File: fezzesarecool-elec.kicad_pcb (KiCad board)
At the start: 2 copper layers, 65 x 56 mm, 62 parts, among them J1 Conn_sel, J14 Conn_LEDs, J15 Audio_input, J18 alim_jacky, J2 Conn_start, J3 CAN_conn, J4 CAN_conn, J5 Conn_01x02, J6 Conn_01x10, J7 alim_5V, P1 Conn_02x20_Odd_Even, Q1 NMOS-T252, Q2 NMOS-T252, Q3 NMOS-T252, U1 MCP2515-EST, U11 MC34152, U12 MC34152, U13 LM4991, U2 TCAN332, U3 SN74AHC1G08, Y1 Crystal_8MHz

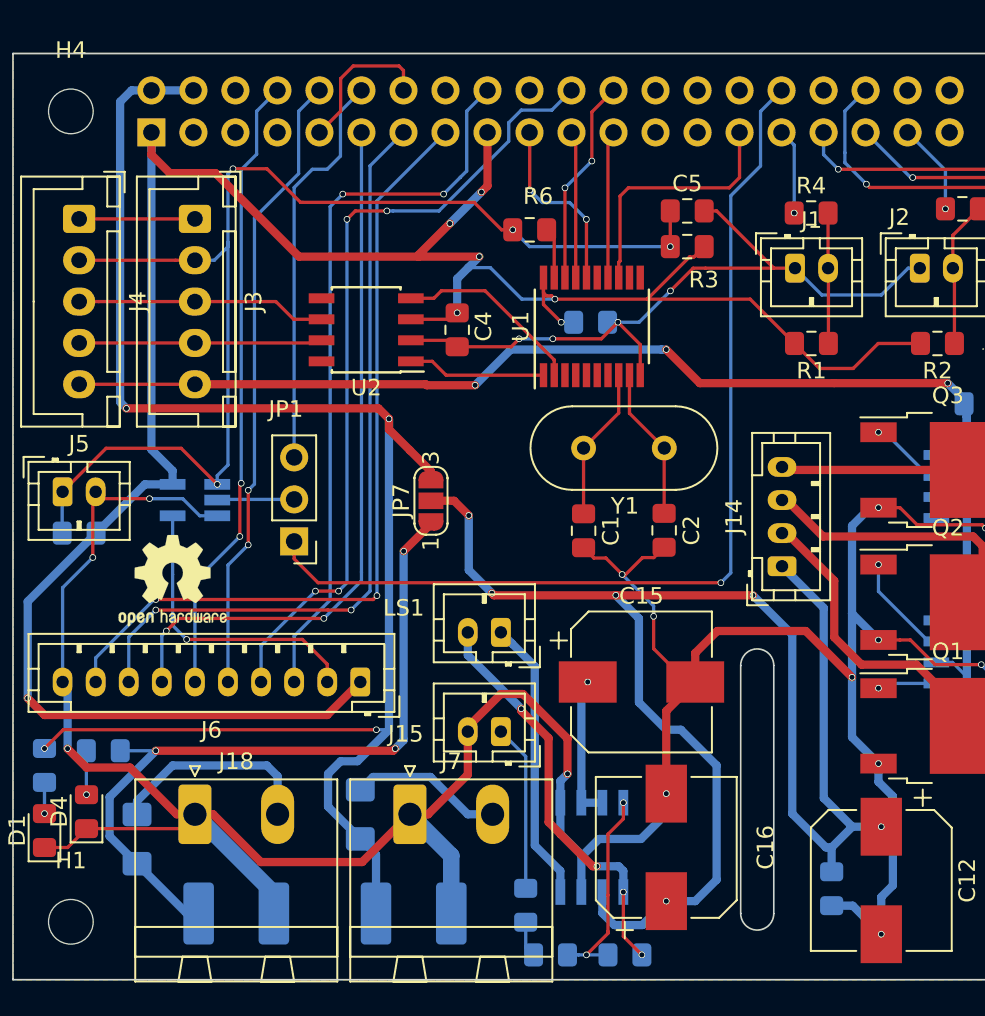
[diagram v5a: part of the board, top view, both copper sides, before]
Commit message: power  tracks corrected
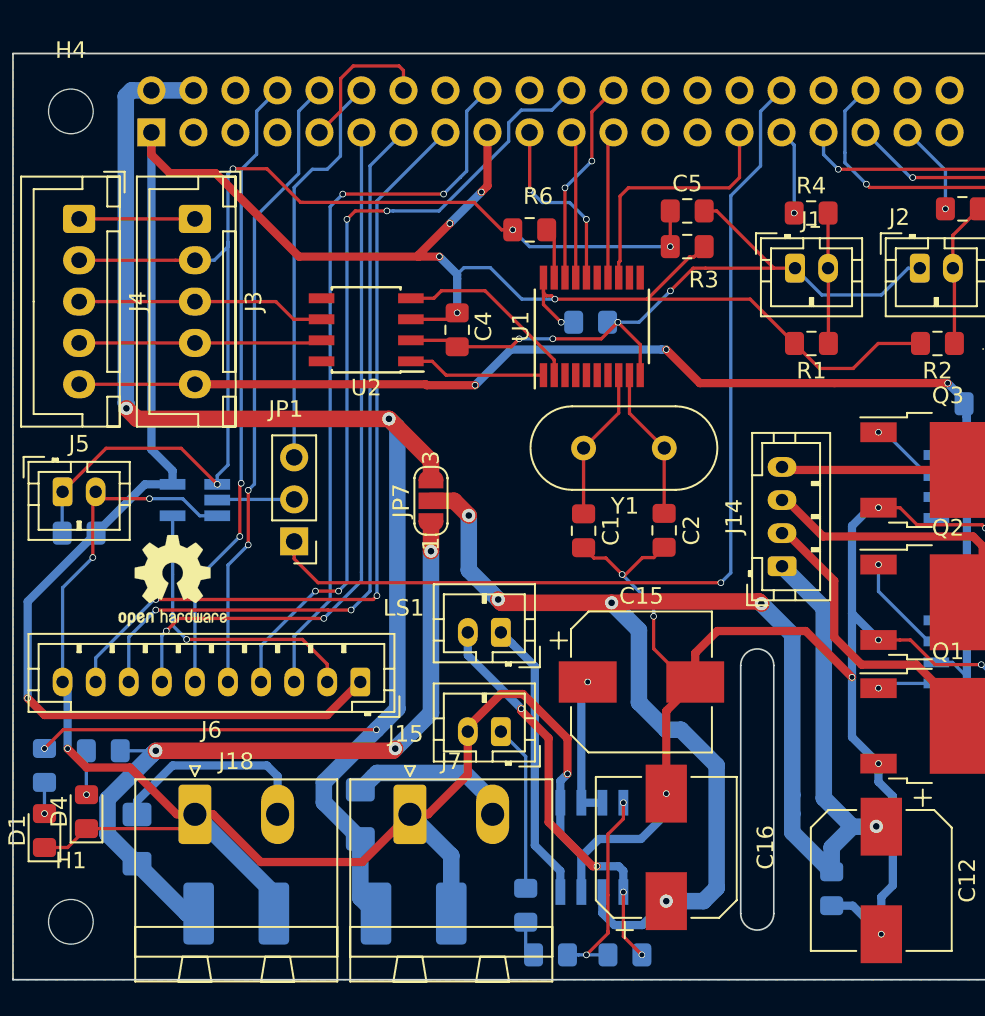
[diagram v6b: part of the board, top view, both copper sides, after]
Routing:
- net +5VD: track 93.6 -> 96.3 mm
- net +3V3: track 141.5 -> 139.8 mm
- net +5V: track 98.8 -> 97.7 mm
- net Net-(F1-Pad1): track 9.26 -> 9.92 mm

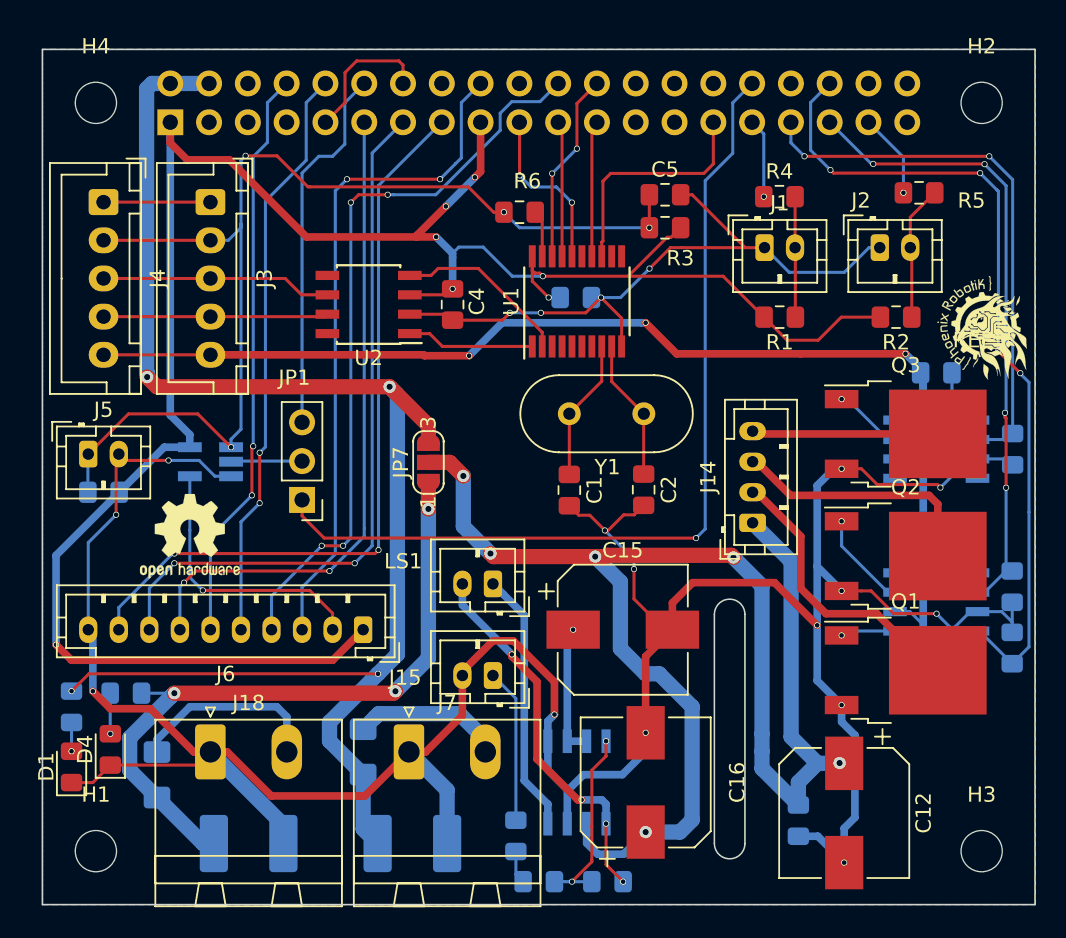
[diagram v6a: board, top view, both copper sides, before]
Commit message: coins arrondis, fix connecteur
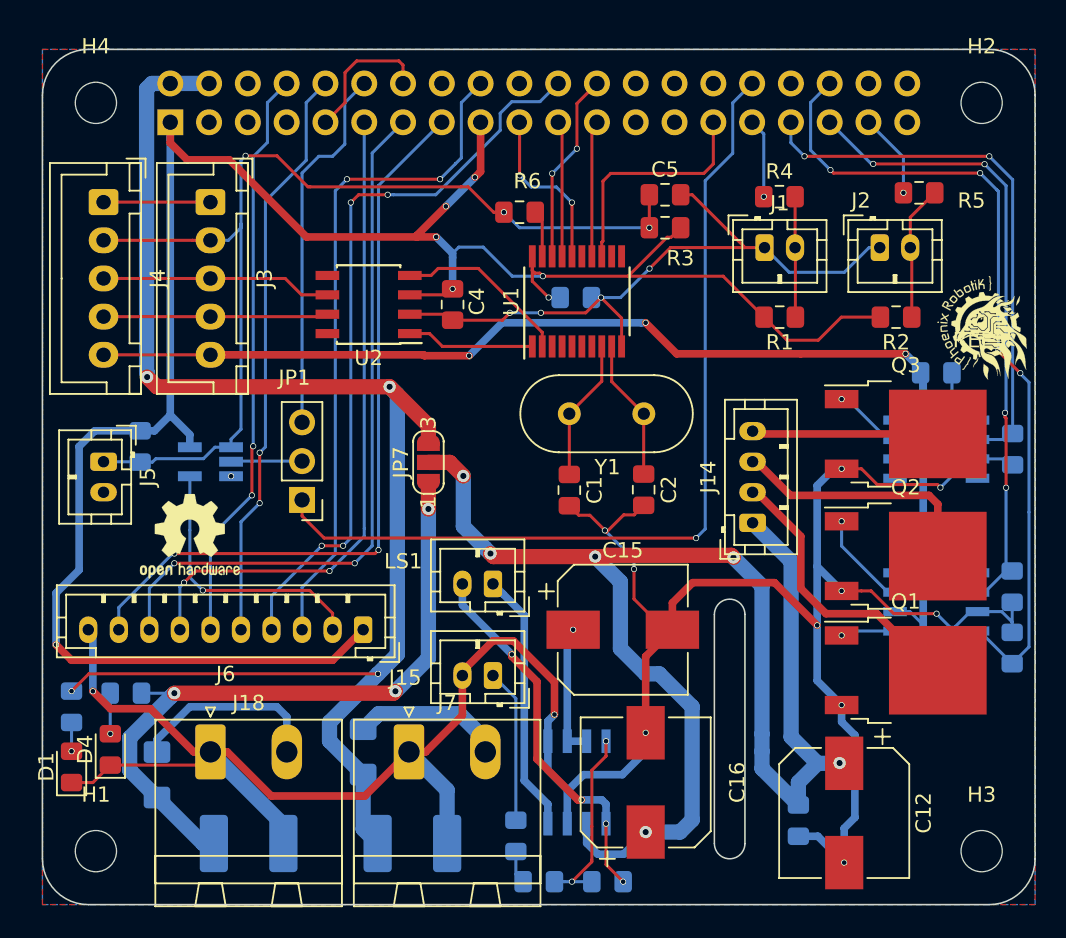
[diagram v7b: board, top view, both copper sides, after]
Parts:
- moved R12 3.84 mm to (206.4, 120.0), turned to 90 degrees
- moved J5 1.12 mm to (204.0, 121.0), turned to 270 degrees
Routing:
- net GND: track 274.9 -> 254.6 mm, vias 18 -> 17
- net /SWD/GRST: track 73.5 -> 68.4 mm, vias 4 -> 3
- net +3V3: track 139.8 -> 142.7 mm
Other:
- outline, holes or cut-outs redrawn
